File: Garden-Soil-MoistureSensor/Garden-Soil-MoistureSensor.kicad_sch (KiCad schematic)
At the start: 7 parts, among them J1 Conn_01x15, J2 Conn_01x15, U1 1043

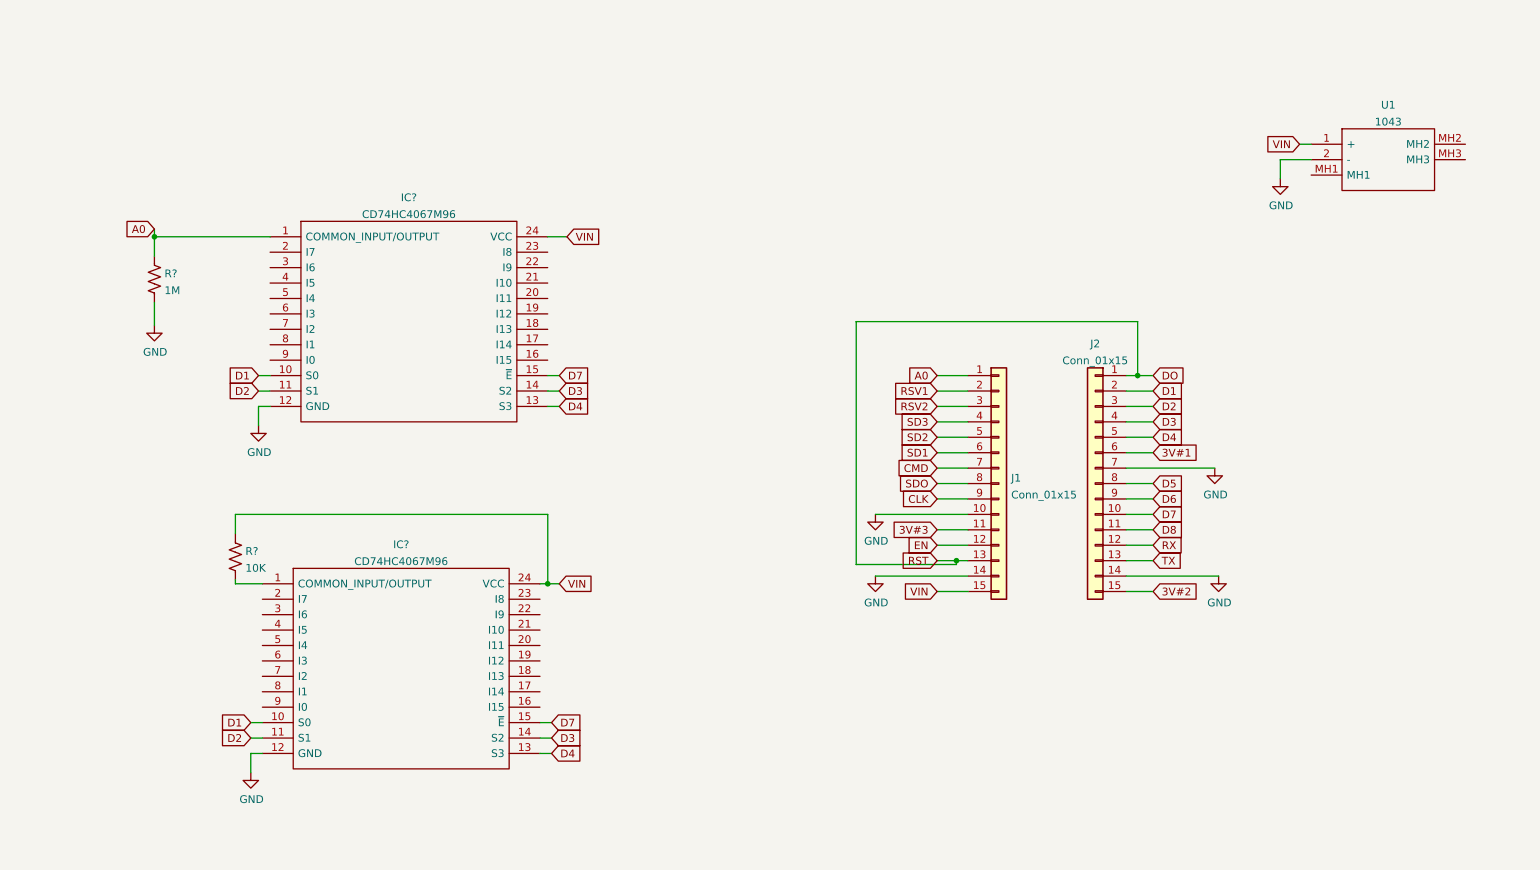
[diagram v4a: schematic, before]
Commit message: autoformat working on MQTT and Wifi connection handling with timeouts. changed sleep duration if can't connect to wifi.
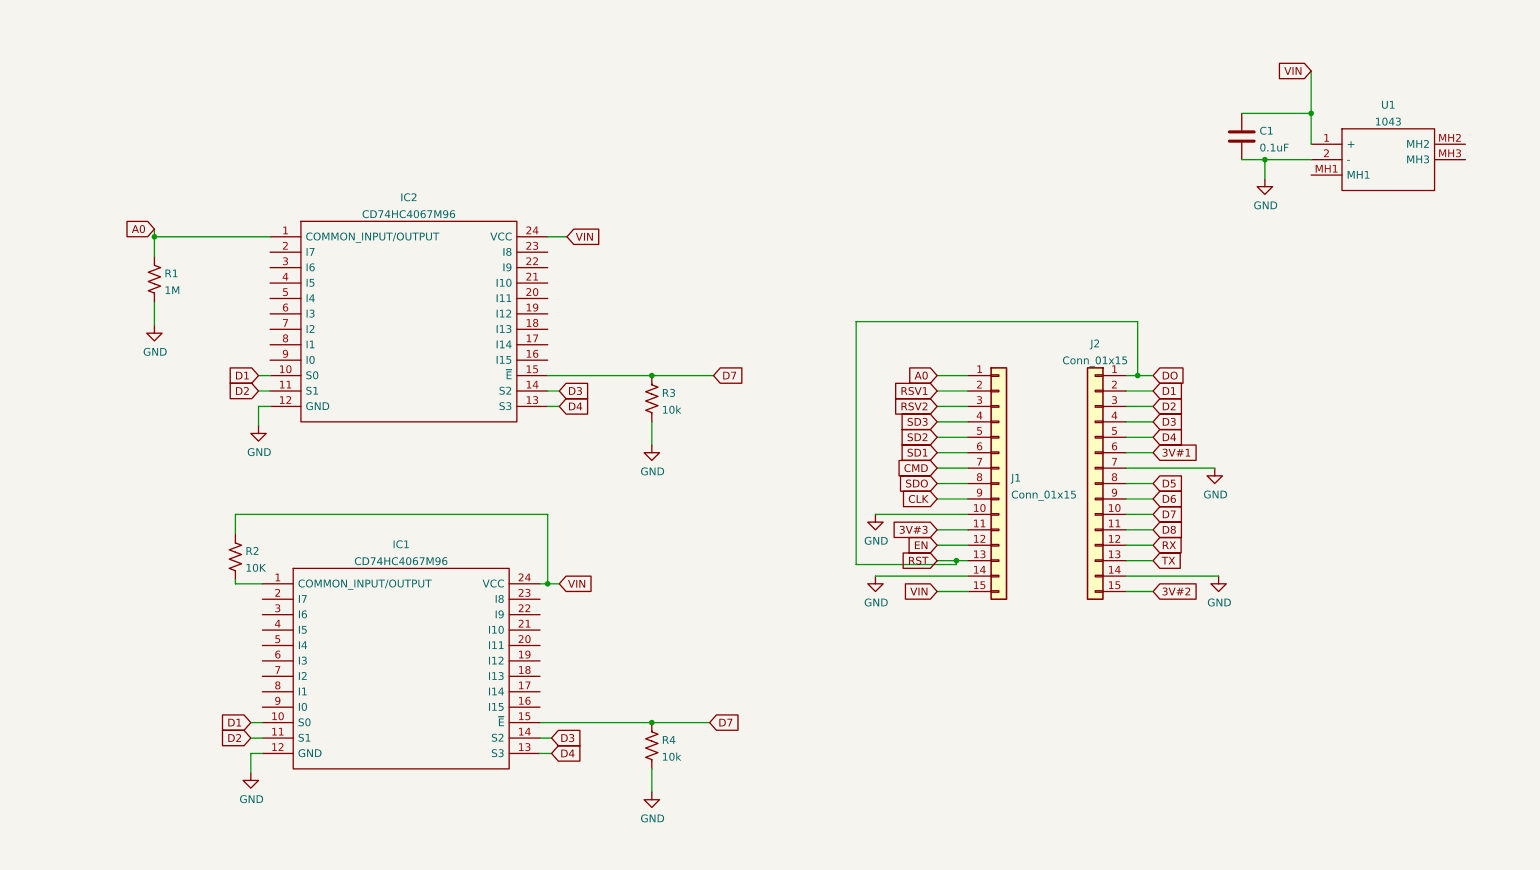
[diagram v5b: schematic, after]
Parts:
- added C1: 0.1uF, symbol Device:C
- added R3, R4: 10k, symbol Device:R_US
- gave numbers to parts that had none: 4
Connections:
- net D7: now also R3.1, R4.1
- net GND: now also C1.2, R3.2, R4.2
- net VIN: now also C1.1

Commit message: got the basics into the schematic. I may rename this model "Liquid Squid" or something like that.
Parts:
- added J3: Conn_02x15_Odd_Even, Connector_PinSocket_2.54mm:PinSocket_2x15_P2.54mm_Horizontal, symbol Connector_Generic:Conn_02x15_Odd_Even
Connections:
- net 15A: now reaches IC2.16 (I15)
- net 15A: now also J3.30 (Pin_30)
- net 14A: now reaches IC2.17 (I14)
- net 14A: now also J3.28 (Pin_28)
- net 13A: now reaches IC2.18 (I13)
- net 13A: now also J3.26 (Pin_26)
- net 12A: now reaches IC2.19 (I12)
- net 12A: now also J3.24 (Pin_24)
- net 7A: now reaches IC2.2 (I7)
- net 7A: now also J3.14 (Pin_14)
- net 11A: now reaches IC2.20 (I11)
- net 11A: now also J3.22 (Pin_22)
- net 10A: now reaches IC2.21 (I10)
- net 10A: now also J3.20 (Pin_20)
- net 9A: now reaches IC2.22 (I9)
- net 9A: now also J3.18 (Pin_18)
- net 8A: now reaches IC2.23 (I8)
- net 8A: now also J3.16 (Pin_16)
- net 6A: now reaches IC2.3 (I6)
- net 6A: now also J3.12 (Pin_12)
- net 5A: now reaches IC2.4 (I5)
- net 5A: now also J3.10 (Pin_10)
- net 4A: now reaches IC2.5 (I4)
- net 4A: now also J3.8 (Pin_8)
- net 3A: now reaches IC2.6 (I3)
- net 3A: now also J3.6 (Pin_6)
- net 2A: now reaches IC2.7 (I2)
- net 2A: now also J3.4 (Pin_4)
- net 1A: now reaches IC2.8 (I1)
- net 1A: now also J3.2 (Pin_2)
- net at IC2.9 (I0): now also IC1.9 (I0)
- net 15B: now reaches IC1.16 (I15)
- net 15B: now also J3.29 (Pin_29)
- net 14B: now reaches IC1.17 (I14)
- net 14B: now also J3.27 (Pin_27)
- net 13B: now reaches IC1.18 (I13)
- net 13B: now also J3.25 (Pin_25)
- net 12B: now reaches IC1.19 (I12)
- net 12B: now also J3.23 (Pin_23)
- net 7B: now reaches IC1.2 (I7)
- net 7B: now also J3.13 (Pin_13)
- net 11B: now reaches IC1.20 (I11)
- net 11B: now also J3.21 (Pin_21)
- net 10B: now reaches IC1.21 (I10)
- net 10B: now also J3.19 (Pin_19)
- net 9B: now reaches IC1.22 (I9)
- net 9B: now also J3.17 (Pin_17)
- net 8B: now reaches IC1.23 (I8)
- net 8B: now also J3.15 (Pin_15)
- net 6B: now reaches IC1.3 (I6)
- net 6B: now also J3.11 (Pin_11)
- net 5B: now reaches IC1.4 (I5)
- net 5B: now also J3.9 (Pin_9)
- net 4B: now reaches IC1.5 (I4)
- net 4B: now also J3.7 (Pin_7)
- net 3B: now reaches IC1.6 (I3)
- net 3B: now also J3.5 (Pin_5)
- net 2B: now reaches IC1.7 (I2)
- net 2B: now also J3.3 (Pin_3)
- net 1B: now reaches IC1.8 (I1)
- net 1B: now also J3.1 (Pin_1)

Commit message: doing some routing and footprint assignments.
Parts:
- C1: footprint (none) -> Capacitor_THT:C_Disc_D6.0mm_W2.5mm_P5.00mm
- IC1, IC2: footprint SOIC127P1030X265-24N -> SamacSys_Parts:SOIC127P1030X265-24N
- R1, R2, R3, R4: footprint (none) -> Resistor_THT:R_Axial_DIN0207_L6.3mm_D2.5mm_P2.54mm_Vertical
- U1: footprint 1043 -> SamacSys_Parts:1043
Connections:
- net GND: now also U1.MH2, U1.MH3
- net VIN: now also U1.MH1
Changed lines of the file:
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@@
   (junction (at 128.27 134.62) (diameter 0) (color 0 0 0 0)
   )
+  (junction (at 265.43 41.91) (diameter 0) (color 0 0 0 0)
+  )
   (junction (at 128.27 77.47) (diameter 0) (color 0 0 0 0)
   )
@@
     (stroke (width 0) (type default) (color 0 0 0 0))
   )
+  (wire (pts (xy 265.43 41.91) (xy 265.43 45.72))
+    (stroke (width 0) (type default) (color 0 0 0 0))
+  )
+  (wire (pts (xy 262.255 39.37) (xy 265.43 39.37))
+    (stroke (width 0) (type default) (color 0 0 0 0))
+  )
   (wire (pts (xy 111.125 64.77) (xy 113.03 64.77))
     (stroke (width 0) (type default) (color 0 0 0 0))
@@
     (stroke (width 0) (type default) (color 0 0 0 0))
   )
+  (wire (pts (xy 265.43 39.37) (xy 265.43 41.91))
+    (stroke (width 0) (type default) (color 0 0 0 0))
+  )
+  (wire (pts (xy 236.855 44.45) (xy 235.585 44.45))
+    (stroke (width 0) (type default) (color 0 0 0 0))
+  )
   (wire (pts (xy 262.255 132.715) (xy 265.43 132.715))
     (stroke (width 0) (type default) (color 0 0 0 0))
@@
     (stroke (width 0) (type default) (color 0 0 0 0))
   )
+  (wire (pts (xy 262.255 41.91) (xy 265.43 41.91))
+    (stroke (width 0) (type default) (color 0 0 0 0))
+  )
   (wire (pts (xy 206.375 110.49) (xy 221.615 110.49))
     (stroke (width 0) (type default) (color 0 0 0 0))
@@
     (stroke (width 0) (type default) (color 0 0 0 0))
   )
+  (wire (pts (xy 235.585 44.45) (xy 235.585 55.245))
+    (stroke (width 0) (type default) (color 0 0 0 0))
+  )
   (wire (pts (xy 62.23 129.54) (xy 64.135 129.54))
     (stroke (width 0) (type default) (color 0 0 0 0))
@@
     (effects (font (size 1.27 1.27)) (justify right))
     (property "Intersheet References" "${INTERSHEET_REFS}" (id 0) (at 242.7574 137.7156 0)
+      (effects (font (size 1.27 1.27)) (justify right) hide)
+    )
+  )
+  (global_label "VIN" (shape input) (at 235.585 55.245 180) (fields_autoplaced)
+    (effects (font (size 1.27 1.27)) (justify right))
+    (property "Intersheet References" "${INTERSHEET_REFS}" (id 0) (at 230.1481 55.1656 0)
       (effects (font (size 1.27 1.27)) (justify right) hide)
     )
@@
     (property "Reference" "IC2" (id 0) (at 88.265 48.1543 0))
     (property "Value" "CD74HC4067M96" (id 1) (at 88.265 50.9294 0))
-    (property "Footprint" "SOIC127P1030X265-24N" (id 2) (at 107.315 52.07 0)
+    (property "Footprint" "SamacSys_Parts:SOIC127P1030X265-24N" (id 2) (at 107.315 52.07 0)
       (effects (font (size 1.27 1.27)) (justify left) hide)
     )
@@
     (property "Reference" "U1" (id 0) (at 249.555 32.9143 0))
     (property "Value" "1043" (id 1) (at 249.555 35.6894 0))
-    (property "Footprint" "1043" (id 2) (at 258.445 36.83 0)
+    (property "Footprint" "SamacSys_Parts:1043" (id 2) (at 258.445 36.83 0)
       (effects (font (size 1.27 1.27)) (justify left) hide)
     )
@@
       (effects (font (size 1.27 1.27)) (justify left))
     )
-    (property "Footprint" "" (id 2) (at 129.286 138.684 90)
+    (property "Footprint" "Resistor_THT:R_Axial_DIN0207_L6.3mm_D2.5mm_P2.54mm_Vertical" (id 2) (at 129.286 138.684 90)
       (effects (font (size 1.27 1.27)) hide)
     )
@@
     (pin "1")
     (pin "2")
+  )
+  (symbol (lib_id "power:GND") (at 265.43 45.72 0) (unit 1)
+    (in_bom yes) (on_board yes)
+    (property "Reference" "#PWR?" (id 0) (at 265.43 52.07 0)
+      (effects (font (size 1.27 1.27)) hide)
+    )
+    (property "Value" "GND" (id 1) (at 265.557 50.1142 0))
+    (property "Footprint" "" (id 2) (at 265.43 45.72 0)
+      (effects (font (size 1.27 1.27)) hide)
+    )
+    (property "Datasheet" "" (id 3) (at 265.43 45.72 0)
+      (effects (font (size 1.27 1.27)) hide)
+    )
+    (pin "1")
   )
   (symbol (lib_id "power:GND") (at 221.615 110.49 0) (unit 1)
@@
       (effects (font (size 1.27 1.27)) (justify left))
     )
-    (property "Footprint" "" (id 2) (at 60.706 107.569 90)
+    (property "Footprint" "Resistor_THT:R_Axial_DIN0207_L6.3mm_D2.5mm_P2.54mm_Vertical" (id 2) (at 60.706 107.569 90)
       (effects (font (size 1.27 1.27)) hide)
     )
@@
       (effects (font (size 1.27 1.27)) (justify left))
     )
-    (property "Footprint" "" (id 2) (at 129.286 81.534 90)
+    (property "Footprint" "Resistor_THT:R_Axial_DIN0207_L6.3mm_D2.5mm_P2.54mm_Vertical" (id 2) (at 129.286 81.534 90)
       (effects (font (size 1.27 1.27)) hide)
     )
@@
       (effects (font (size 1.27 1.27)) (justify left))
     )
-    (property "Footprint" "" (id 2) (at 47.371 61.849 90)
+    (property "Footprint" "Resistor_THT:R_Axial_DIN0207_L6.3mm_D2.5mm_P2.54mm_Vertical" (id 2) (at 47.371 61.849 90)
       (effects (font (size 1.27 1.27)) hide)
     )
@@
     (property "Reference" "IC1" (id 0) (at 86.995 105.3043 0))
     (property "Value" "CD74HC4067M96" (id 1) (at 86.995 108.0794 0))
-    (property "Footprint" "SOIC127P1030X265-24N" (id 2) (at 106.045 109.22 0)
+    (property "Footprint" "SamacSys_Parts:SOIC127P1030X265-24N" (id 2) (at 106.045 109.22 0)
       (effects (font (size 1.27 1.27)) (justify left) hide)
     )
@@
       (effects (font (size 1.27 1.27)) (justify left))
     )
-    (property "Footprint" "" (id 2) (at 226.3902 41.91 0)
+    (property "Footprint" "Capacitor_THT:C_Disc_D6.0mm_W2.5mm_P5.00mm" (id 2) (at 226.3902 41.91 0)
       (effects (font (size 1.27 1.27)) hide)
     )
@@
       (reference "#PWR0101") (unit 1) (value "GND") (footprint "")
     )
+    (path "/66de9b46-c597-4831-afb6-ee7cf817c679"
+      (reference "#PWR?") (unit 1) (value "GND") (footprint "")
+    )
     (path "/f0efd7d9-5329-435f-b120-2377b48fb3c9"
-      (reference "C1") (unit 1) (value "0.1uF") (footprint "")
+      (reference "C1") (unit 1) (value "0.1uF") (footprint "Capacitor_THT:C_Disc_D6.0mm_W2.5mm_P5.00mm")
     )
     (path "/e11f20a4-269e-40f6-acea-5a1ced4c7672"
-      (reference "IC1") (unit 1) (value "CD74HC4067M96") (footprint "SOIC127P1030X265-24N")
+      (reference "IC1") (unit 1) (value "CD74HC4067M96") (footprint "SamacSys_Parts:SOIC127P1030X265-24N")
     )
     (path "/43d1f199-f4ee-4683-993f-3ccce3985416"
-      (reference "IC2") (unit 1) (value "CD74HC4067M96") (footprint "SOIC127P1030X265-24N")
+      (reference "IC2") (unit 1) (value "CD74HC4067M96") (footprint "SamacSys_Parts:SOIC127P1030X265-24N")
     )
     (path "/c24d6ac8-802d-4df3-a210-9cb1f693e865"
@@
     )
     (path "/d90db84e-7df3-4d1b-b263-27f7c3991121"
-      (reference "R1") (unit 1) (value "1M") (footprint "")
+      (reference "R1") (unit 1) (value "1M") (footprint "Resistor_THT:R_Axial_DIN0207_L6.3mm_D2.5mm_P2.54mm_Vertical")
     )
     (path "/96ff3848-eccf-424d-a5fe-891878a062a1"
-      (reference "R2") (unit 1) (value "10K") (footprint "")
+      (reference "R2") (unit 1) (value "10K") (footprint "Resistor_THT:R_Axial_DIN0207_L6.3mm_D2.5mm_P2.54mm_Vertical")
     )
     (path "/cd5bf8b2-7451-4e1b-9de1-fae653e0d5ac"
-      (reference "R3") (unit 1) (value "10k") (footprint "")
+      (reference "R3") (unit 1) (value "10k") (footprint "Resistor_THT:R_Axial_DIN0207_L6.3mm_D2.5mm_P2.54mm_Vertical")
     )
     (path "/6281ebbb-35e7-4c8d-ad07-5d6ab74e0763"
-      (reference "R4") (unit 1) (value "10k") (footprint "")
+      (reference "R4") (unit 1) (value "10k") (footprint "Resistor_THT:R_Axial_DIN0207_L6.3mm_D2.5mm_P2.54mm_Vertical")
     )
     (path "/5b70b09b-6762-4725-9d48-805300c0bdc8"
-      (reference "U1") (unit 1) (value "1043") (footprint "1043")
-    )
-  )
+      (reference "U1") (unit 1) (value "1043") (footprint "SamacSys_Parts:1043")
+    )
+  )
